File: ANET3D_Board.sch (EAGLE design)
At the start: 201 parts, among them J3 J3, J7 (DNP), J9 USB Type-B, Q1 IRLR7843PbF, Q2 IRLR7843PbF, Q3 IRLR7843PbF, Q4 L7805CD, SW1 RESET, T1 TPTP09R, T10 TPTP09R, T11 TPTP09R, T12 TPTP09R, T13 TPTP09R, T14 TPTP09R, T15 TPTP09R, T16 TPTP09R, T17 TPTP09R, T18 TPTP09R, T19 TPTP09R, T2 TPTP09R, T20 TPTP09R, T21 TPTP09R, T22 TPTP09R, T23 TPTP09R, T24 TPTP09R, T25 TPTP09R, T26 TPTP09R, T27 TPTP09R, T28 TPTP09R, T29 TPTP09R, T3 TPTP09R, T30 TPTP09R, T31 TPTP09R, T32 TPTP09R, T33 TPTP09R, T34 TPTP09R, T35 TPTP09R, T36 TPTP09R, T37 TPTP09R, T38 TPTP09R, T39 TPTP09R, T4 TPTP09R, T40 TPTP09R, T41 TPTP09R, T42 TPTP09R, T43 TPTP09R, T44 TPTP09R, T45 TPTP09R, T46 TPTP09R, T47 TPTP09R, T48 TPTP09R, T49 TPTP09R, T5 TPTP09R, T50 TPTP09R, T51 TPTP09R, T52 TPTP09R, T53 TPTP09R, T54 TPTP09R, T55 TPTP09R, T56 TPTP09R, T57 TPTP09R, T58 TPTP09R, T59 TPTP09R, T6 TPTP09R, T60 TPTP09R, T61 TPTP09R, T62 TPTP09R, T7 TPTP09R, T8 TPTP09R, T9 TPTP09R, U1 A4988, U10 AMS1117-3.3, U2 A4988, U3 A4988, U4 A4988, U5 ATMEGA1284P, U6 CH340G, U8 4050D, Y1 16MHz, Y2 12MHz

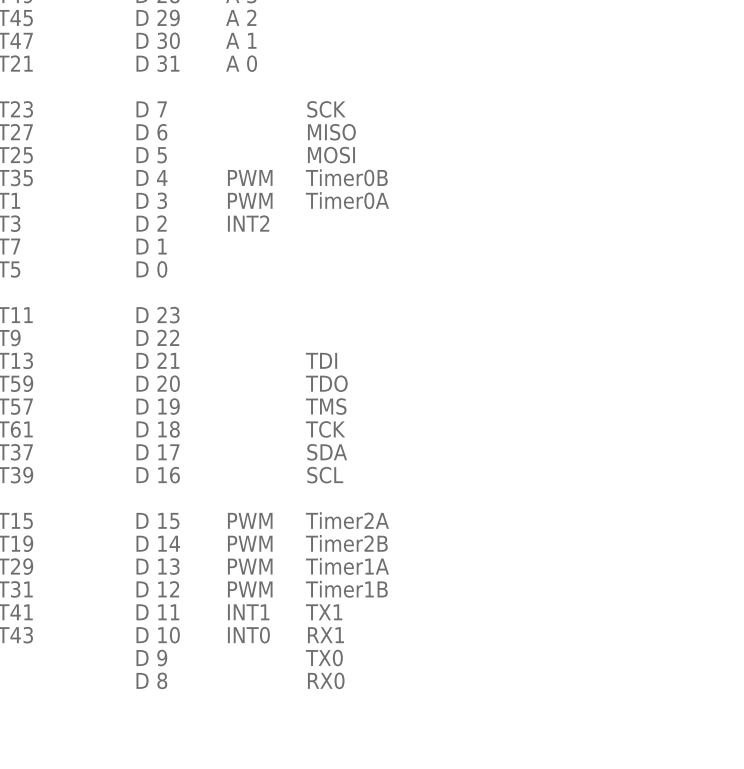
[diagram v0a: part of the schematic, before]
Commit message: Arduino Pin definition added (for NAET 3D Board LED D1 (LED_BUILTIN))
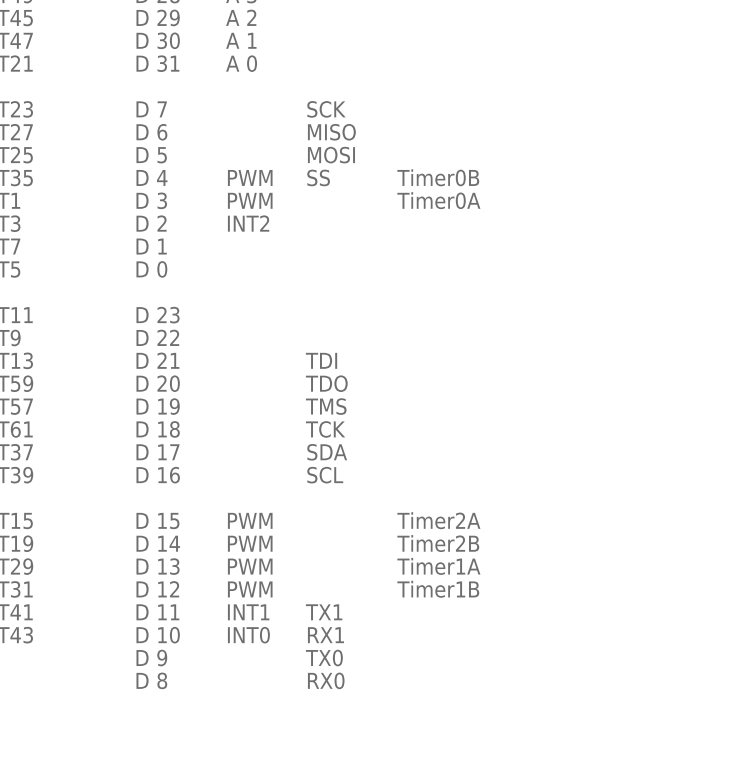
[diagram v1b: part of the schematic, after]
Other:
- note added: "SS"
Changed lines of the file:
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@@
 <setting verticaltext="up"/>
 </settings>
-<grid distance="25" unitdist="mil" unit="mil" style="dots" multiple="2" display="yes" altdistance="0.01" altunitdist="inch" altunit="inch"/>
+<grid distance="0.1" unitdist="inch" unit="inch" style="lines" multiple="1" display="yes" altdistance="0.01" altunitdist="inch" altunit="inch"/>
 <layers>
 <layer number="1" name="Top" color="4" fill="1" visible="no" active="no"/>
@@
 <text x="445.77" y="62.23" size="1.778" layer="95">D 8</text>
 <text x="445.77" y="148.59" size="1.778" layer="95">D 24</text>
-<text x="464.82" y="115.57" size="1.778" layer="95">Timer0A</text>
-<text x="464.82" y="118.11" size="1.778" layer="95">Timer0B</text>
-<text x="464.82" y="72.39" size="1.778" layer="95">Timer1B</text>
-<text x="464.82" y="74.93" size="1.778" layer="95">Timer1A</text>
-<text x="464.82" y="77.47" size="1.778" layer="95">Timer2B</text>
-<text x="464.82" y="80.01" size="1.778" layer="95">Timer2A</text>
+<text x="474.98" y="115.57" size="1.778" layer="95">Timer0A</text>
+<text x="474.98" y="118.11" size="1.778" layer="95">Timer0B</text>
+<text x="474.98" y="72.39" size="1.778" layer="95">Timer1B</text>
+<text x="474.98" y="74.93" size="1.778" layer="95">Timer1A</text>
+<text x="474.98" y="77.47" size="1.778" layer="95">Timer2B</text>
+<text x="474.98" y="80.01" size="1.778" layer="95">Timer2A</text>
 <text x="464.82" y="120.65" size="1.778" layer="95">MOSI</text>
 <text x="464.82" y="123.19" size="1.778" layer="95">MISO</text>
@@
 <text x="455.93" y="69.85" size="1.778" layer="95">INT1</text>
 <text x="455.93" y="67.31" size="1.778" layer="95">INT0</text>
+<text x="464.82" y="118.11" size="1.778" layer="95">SS</text>
 </plain>
 <instances>

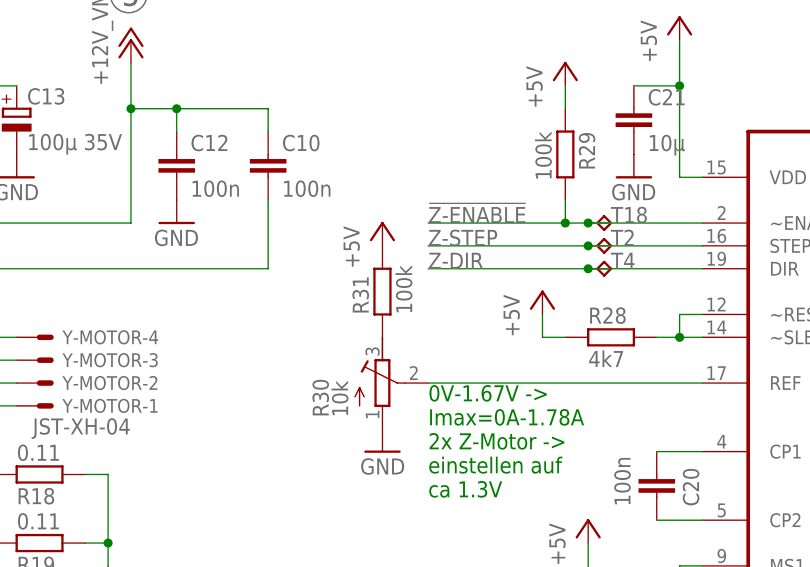
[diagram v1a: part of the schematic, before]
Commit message: value R31 corrected
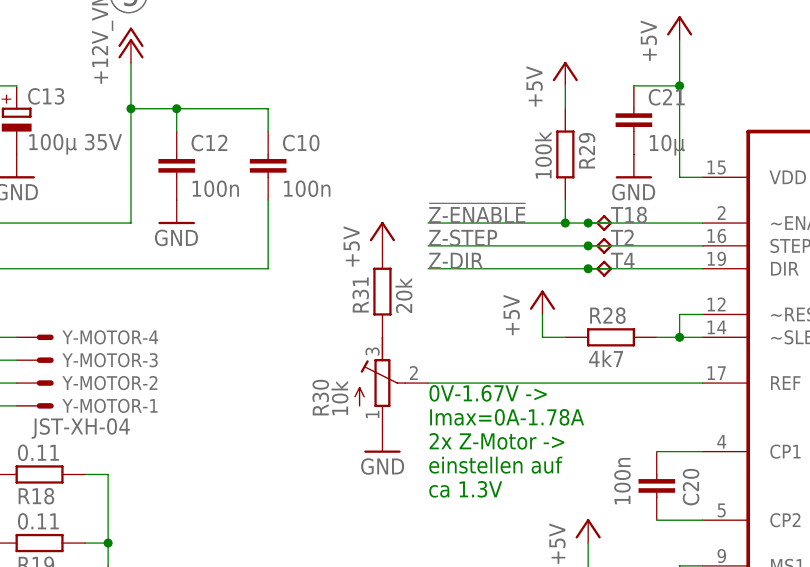
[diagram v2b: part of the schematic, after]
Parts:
- R31: value 100k -> 20k
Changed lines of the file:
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@@
 <setting verticaltext="up"/>
 </settings>
-<grid distance="0.1" unitdist="inch" unit="inch" style="lines" multiple="1" display="yes" altdistance="0.01" altunitdist="inch" altunit="inch"/>
+<grid distance="0.1" unitdist="inch" unit="inch" style="lines" multiple="1" display="no" altdistance="0.01" altunitdist="inch" altunit="inch"/>
 <layers>
 <layer number="1" name="Top" color="4" fill="1" visible="no" active="no"/>
@@
 <part name="C21" library="rcl" deviceset="C-EU" device="C0805" value="10µ"/>
 <part name="GND57" library="SparkFun" deviceset="GND" device=""/>
-<part name="R31" library="ipc-7351-resistor" deviceset="RESISTOR_" device="0805" value="100k"/>
+<part name="R31" library="ipc-7351-resistor" deviceset="RESISTOR_" device="0805" value="20k"/>
 <part name="GND58" library="SparkFun" deviceset="GND" device=""/>
 <part name="P+23" library="supply1" deviceset="+5V" device=""/>
